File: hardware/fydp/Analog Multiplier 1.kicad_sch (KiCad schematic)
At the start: 24 parts, among them J8 Conn_01x02_Pin, U1 LTC2630ISC6-LZ8-TRMPBF, U2 AD633ARZ-R7, U3 SN74LVC1G3157DCKR, U4 LTC2630ISC6-LZ8-TRMPBF, U5 SN74LVC1G3157DCKR, U6 AD633ARZ-R7

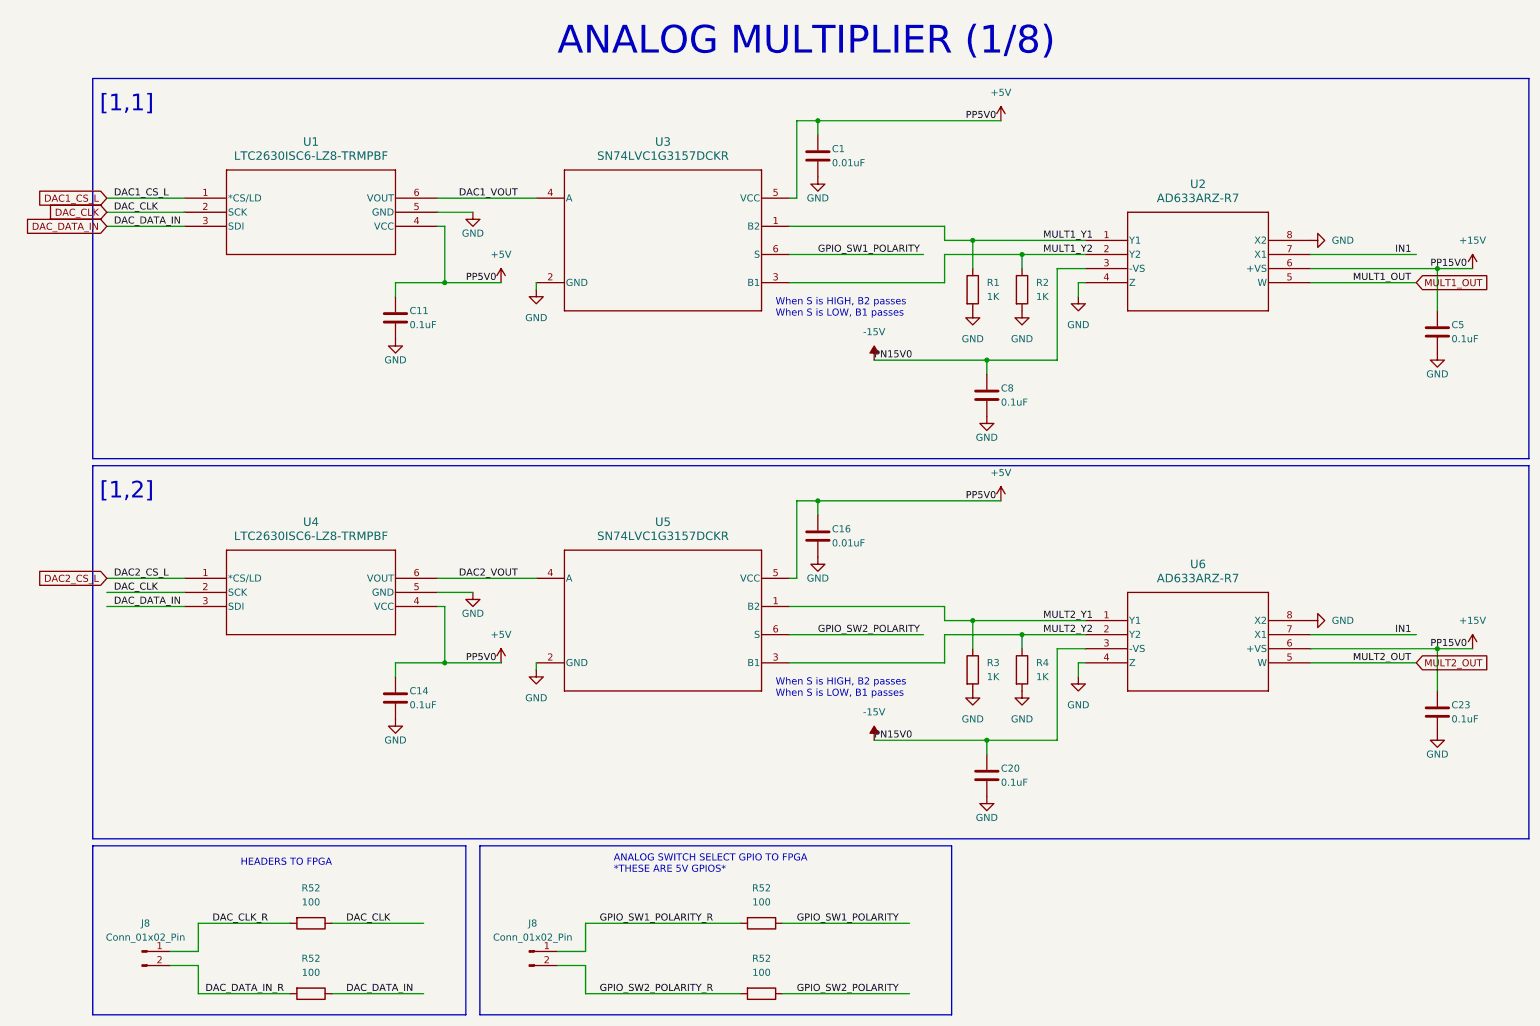
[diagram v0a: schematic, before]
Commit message: Remove 2 channels of multiplier and change ADC
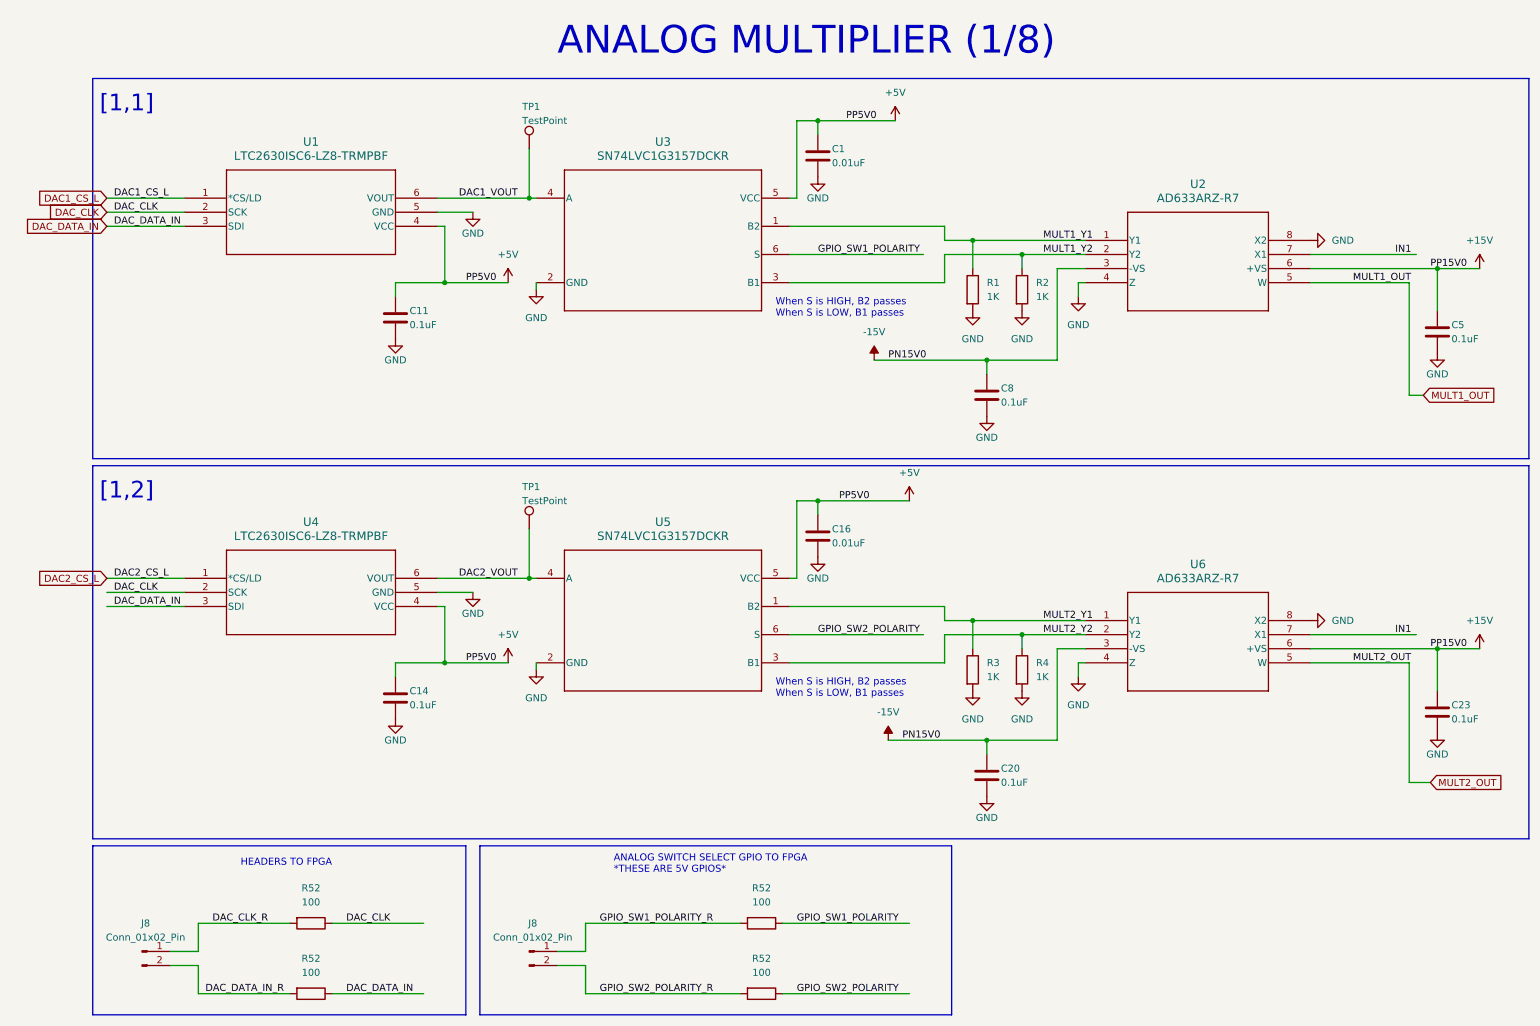
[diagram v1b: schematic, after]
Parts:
- added TP1 (x2): TestPoint, TestPoint:TestPoint_Pad_1.0x1.0mm, symbol Connector:TestPoint
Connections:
- net DAC1_VOUT: now also TP1.1
- net DAC2_VOUT: now also TP1.1

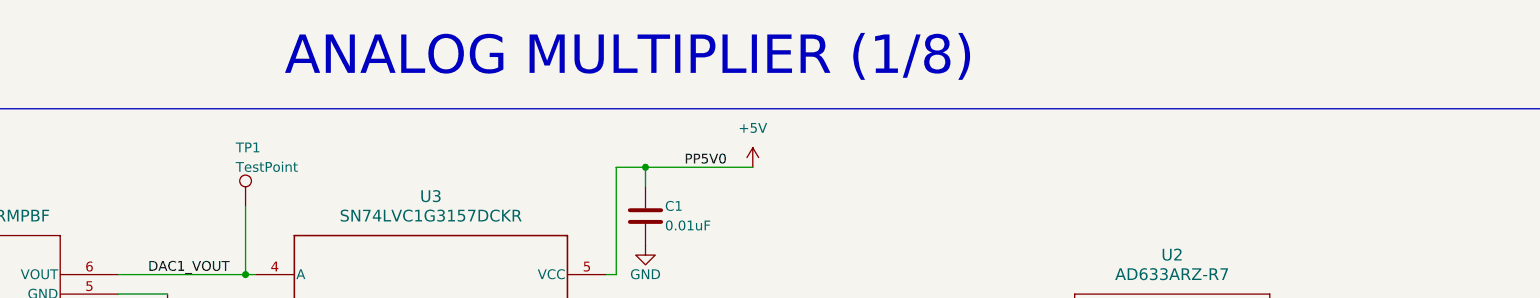
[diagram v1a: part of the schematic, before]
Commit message: Edit schematic titles
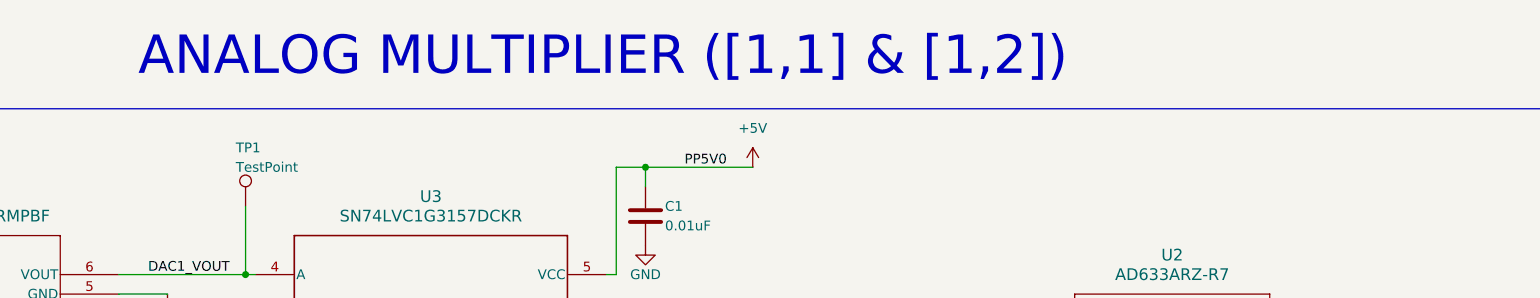
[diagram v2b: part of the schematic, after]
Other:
- note added: "ANALOG MULTIPLIER ([1,1] & [1,2])"
- note removed: "ANALOG MULTIPLIER (1/8)"
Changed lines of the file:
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@@
     (effects (font (size 1.27 1.27)) (justify left bottom))
   )
-  (text "ANALOG MULTIPLIER (1/8)" (at 102.87 22.86 0)
+  (text "ANALOG MULTIPLIER ([1,1] & [1,2])" (at 83.82 22.86 0)
     (effects (font (size 5 5)) (justify left bottom))
   )

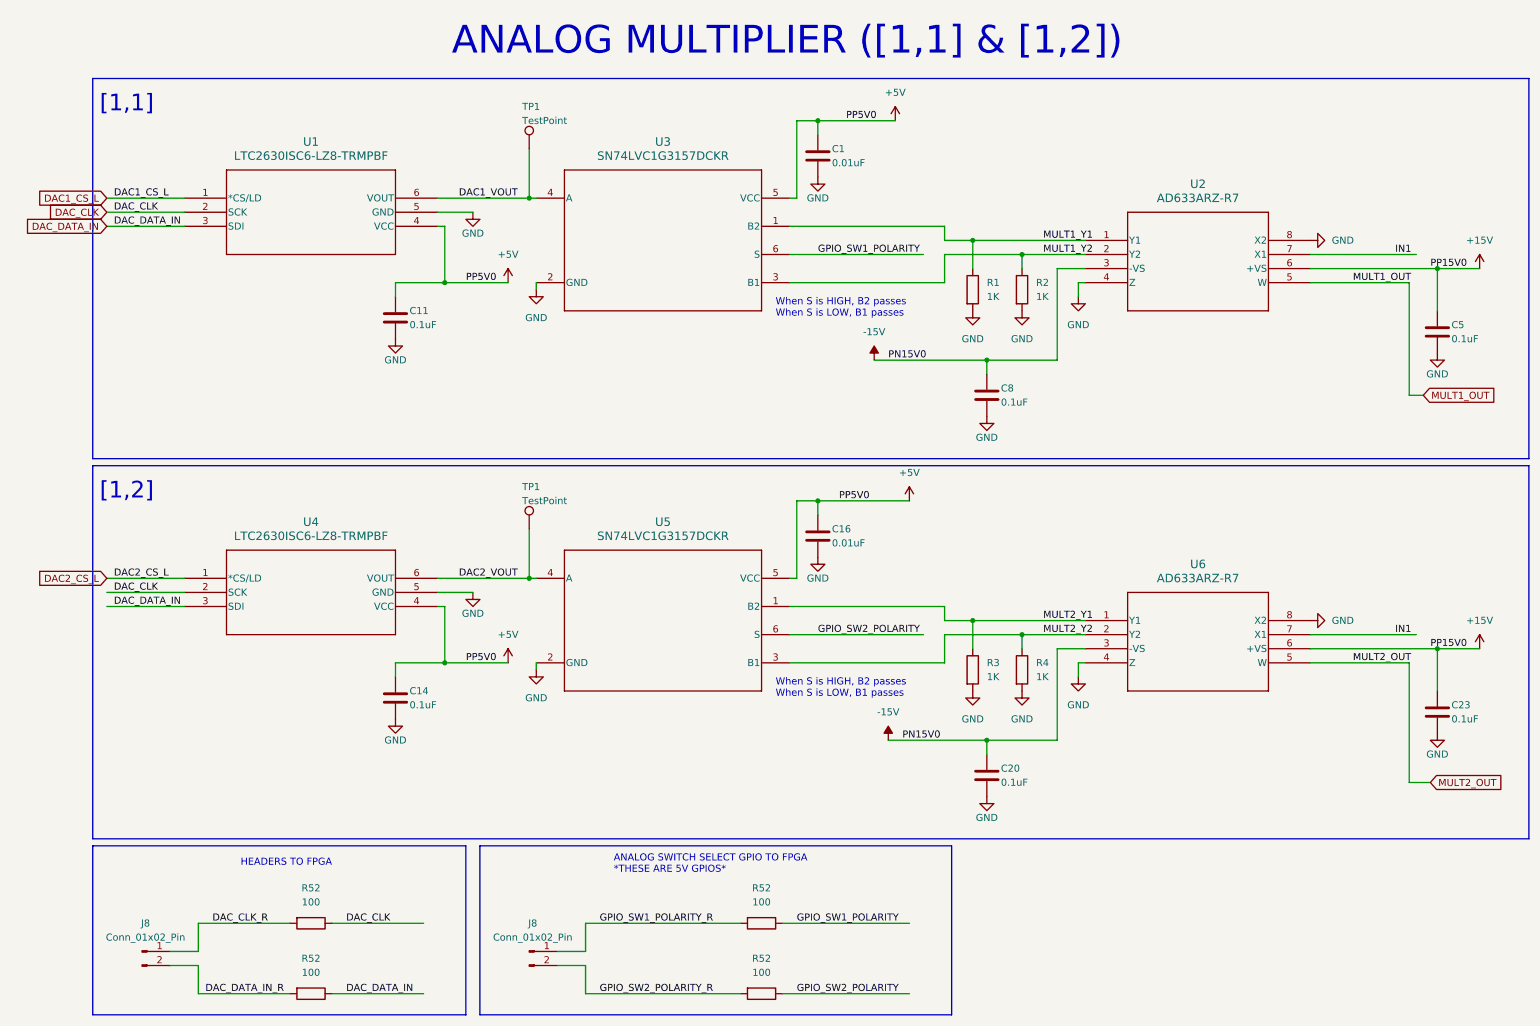
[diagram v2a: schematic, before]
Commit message: Initial layout mostly complete, need to complete lots of routing
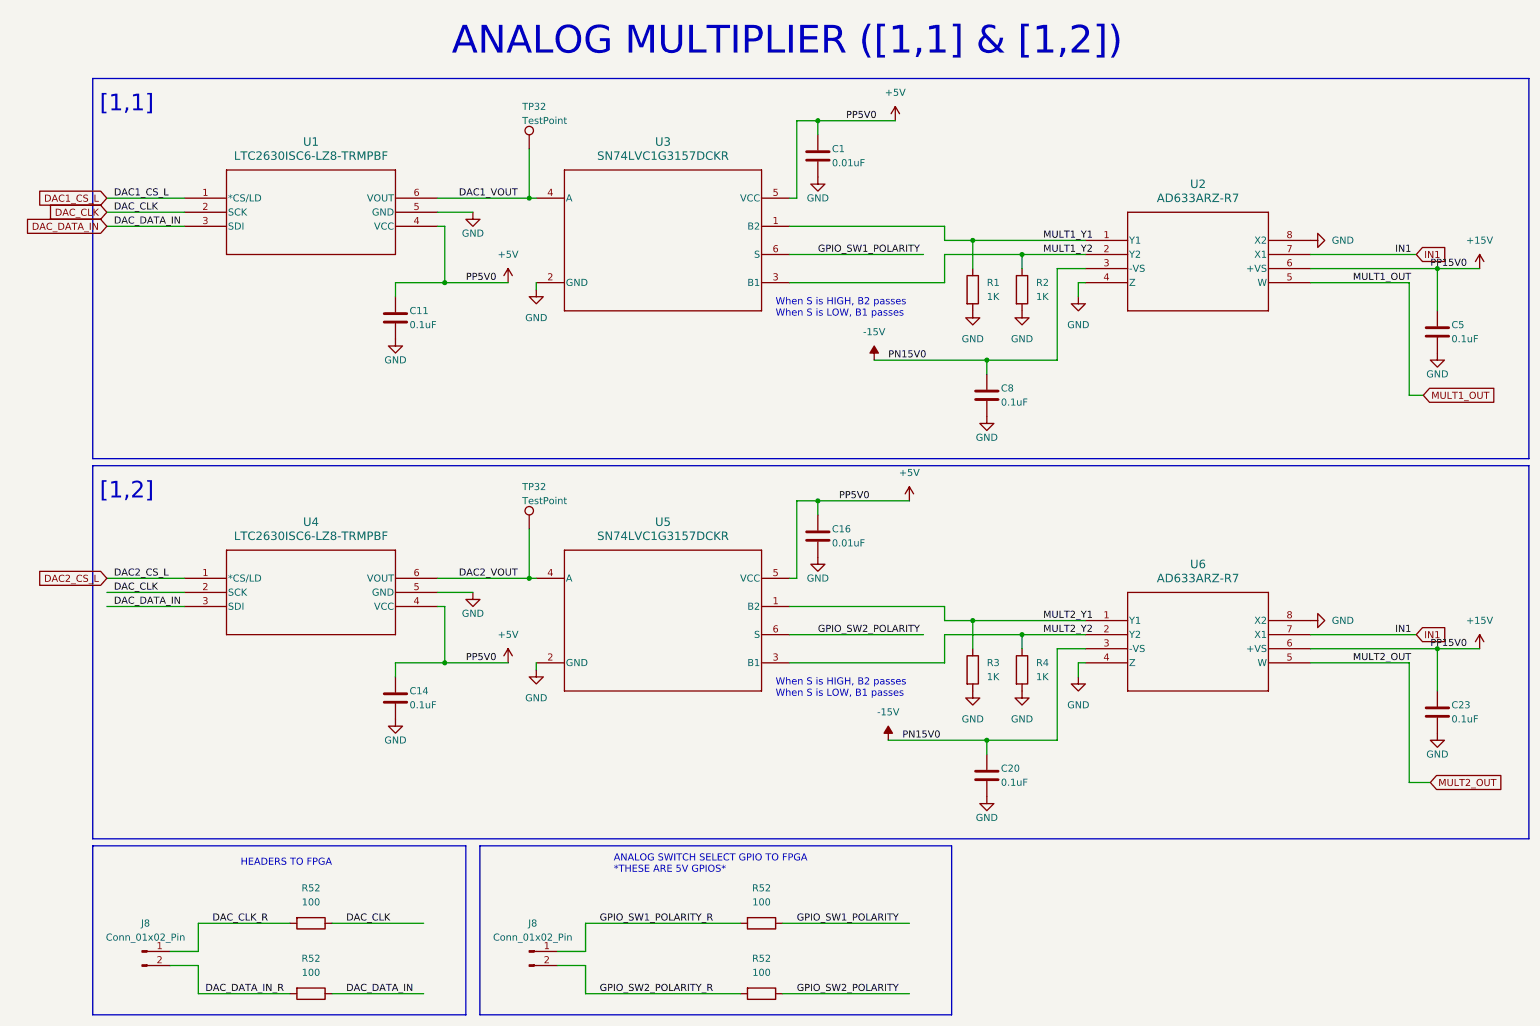
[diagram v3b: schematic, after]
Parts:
- renumbered TP1 to TP32
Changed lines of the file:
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@@
+    )
+  )
+  (global_label "IN1" (shape input) (at 257.81 58.42 0) (fields_autoplaced)
+    (effects (font (size 1.27 1.27)) (justify left))
+    (property "Intersheetrefs" "${INTERSHEET_REFS}" (at 263.94 58.42 0)
+      (effects (font (size 1.27 1.27)) (justify left) hide)
     )
   )
@@
     )
   )
+  (global_label "IN1" (shape input) (at 257.81 127 0) (fields_autoplaced)
+    (effects (font (size 1.27 1.27)) (justify left))
+    (property "Intersheetrefs" "${INTERSHEET_REFS}" (at 263.94 127 0)
+      (effects (font (size 1.27 1.27)) (justify left) hide)
+    )
+  )
   (global_label "DAC1_CS_L" (shape input) (at 21.59 48.26 180) (fields_autoplaced)
     (effects (font (size 1.27 1.27)) (justify right))
@@
   (symbol (lib_id "Connector:TestPoint") (at 97.79 39.37 0) (unit 1)
     (in_bom yes) (on_board yes) (dnp no)
-    (property "Reference" "TP1" (at 96.52 31.75 0)
+    (property "Reference" "TP32" (at 96.52 31.75 0)
       (effects (font (size 1.27 1.27)) (justify left))
     )
@@
   (symbol (lib_id "Connector:TestPoint") (at 97.79 107.95 0) (unit 1)
     (in_bom yes) (on_board yes) (dnp no)
-    (property "Reference" "TP1" (at 96.52 100.33 0)
-      (effects (font (size 1.27 1.27)) (justify left))
-    )
+    (property "Reference" "TP32" (at 96.52 100.33 0)
+      (effects (font (size 1.27 1.27)) (justify left))
+    )

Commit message: Completed placement and silk for left and centre sections of the PCB
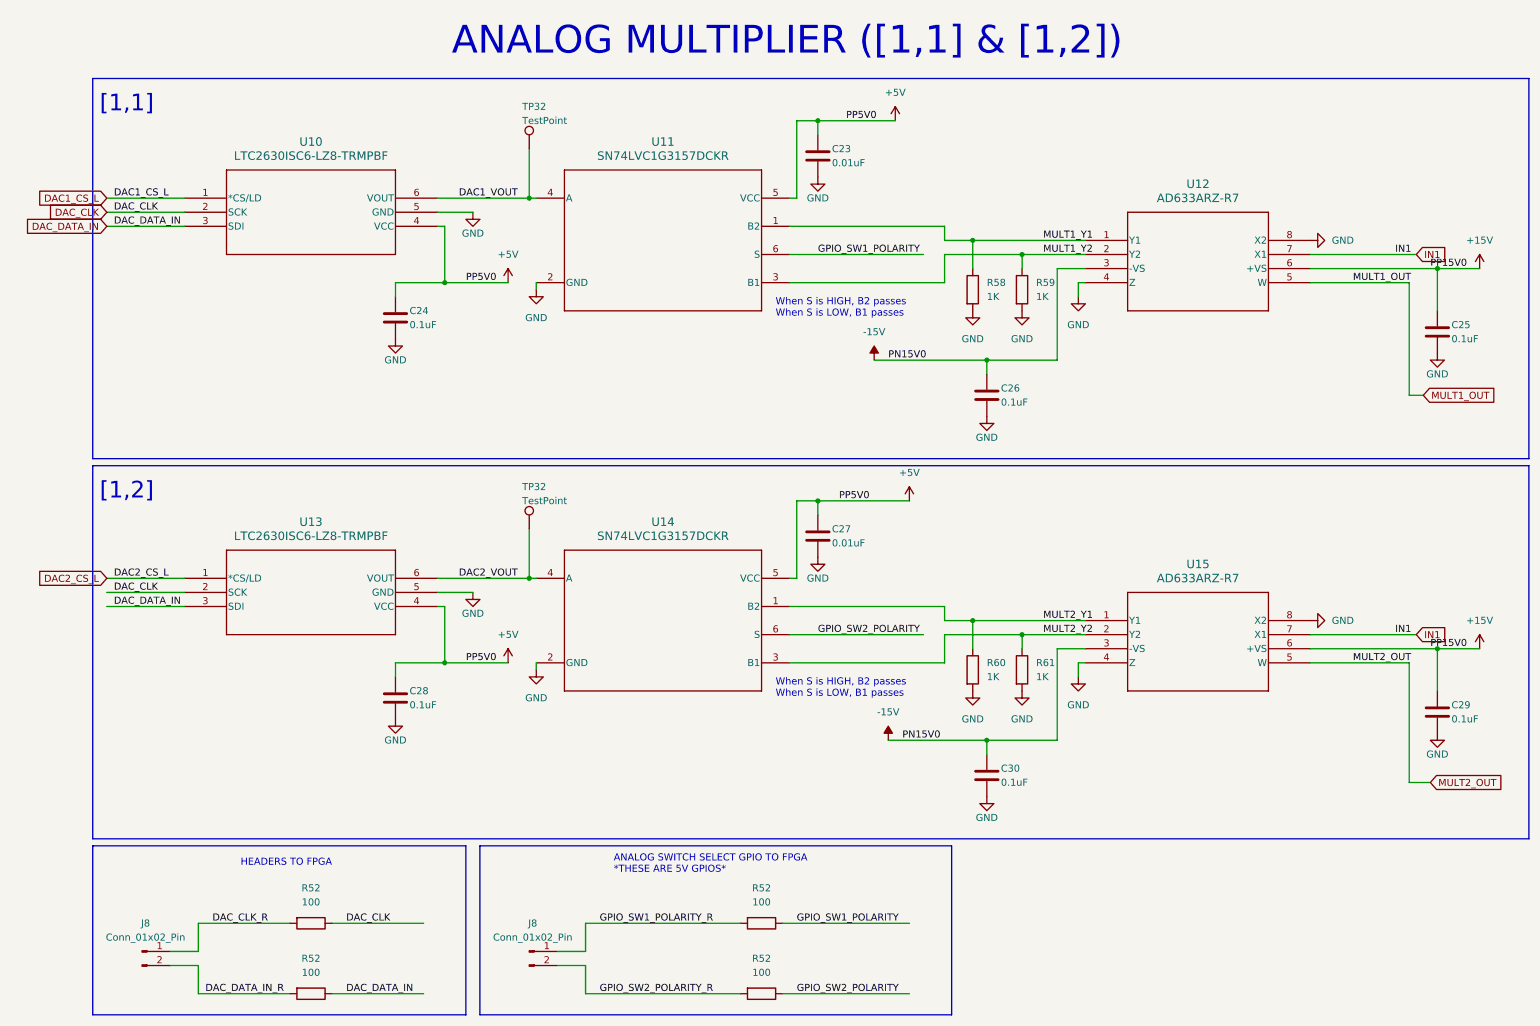
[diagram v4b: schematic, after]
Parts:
- renumbered C1 to C23, C11 to C24, C5 to C25, C8 to C26, C16 to C27, C14 to C28, C23 to C29, C20 to C30, R1 to R58, R2 to R59, R3 to R60, R4 to R61, U1 to U10, U3 to U11, U2 to U12, U4 to U13, U5 to U14, U6 to U15
